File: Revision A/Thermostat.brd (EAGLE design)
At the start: 75.9 x 52.1 mm, 22 parts

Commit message: Custom Components
Designed custom components for the temperature sensor and switching
regulator.  Corrected pin 42 to 46.  Corrected some mistakes in the
schematic and re-arranged it.  Rewired the board paths to match the
original published directions.  Have not tested printing or alignment
yet.
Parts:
- removed TEMP: (no value), SparkFun-Sensors:TO-92
- removed V7815W: 7815T, linear:TO220H
- added U$1: TMP36, android-thermostat:TMP36
- added U$2: V715W-500R, android-thermostat:SWITCHINGREGULATOR
- moved 10U 7.73 mm to (61.0, 36.8), turned to 270 degrees
- moved RECT 4.02 mm to (39.4, 43.2)
- moved 100U 1.27 mm to (47.0, 36.8)
- renumbered P-42 to P-46
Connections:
- removed net N$13 (its old number): 100U.1, RECT.+, V7815W.3
- new net N$5: P-46.1, U$1.DATA-2
- net GND: now also U$1.GND-3, U$2.GND; no longer TEMP.3, V7815W.2
- net N$10: now also 10U.1, P-VIN.1, U$2.VO; no longer P-46.1, TEMP.2
- net N$11: now also U$1.VCC-1; no longer TEMP.1
- net N$12: now also 100U.1, RECT.+, U$2.VI; no longer 10U.1, P-VIN.1, V7815W.1
- net N$3: now also RECT.AC1; no longer RECT.AC2
- net P2: now also RECT.AC2; no longer RECT.AC1
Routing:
- net GND: track 132.6 -> 188.0 mm
- net N$12: track 46.0 -> 17.8 mm
- net N$5: track 0.00 -> 25.4 mm
- net N$13 (its old number): track 17.8 -> 0.00 mm
- net N$10: track 34.9 -> 17.8 mm
- net N$3: track 30.7 -> 40.6 mm
- net P2: track 69.6 -> 78.7 mm
- net N$1: track 32.1 -> 38.1 mm
- net N$4: track 8.13 -> 11.4 mm
- net N$13: track 35.1 -> 38.1 mm
- net N$15: track 30.8 -> 33.0 mm
- net N$14: track 25.7 -> 27.9 mm
- net N$7: track 15.0 -> 16.5 mm
- net N$11: track 8.89 -> 7.62 mm
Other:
- board text added: "Android Thermostat"

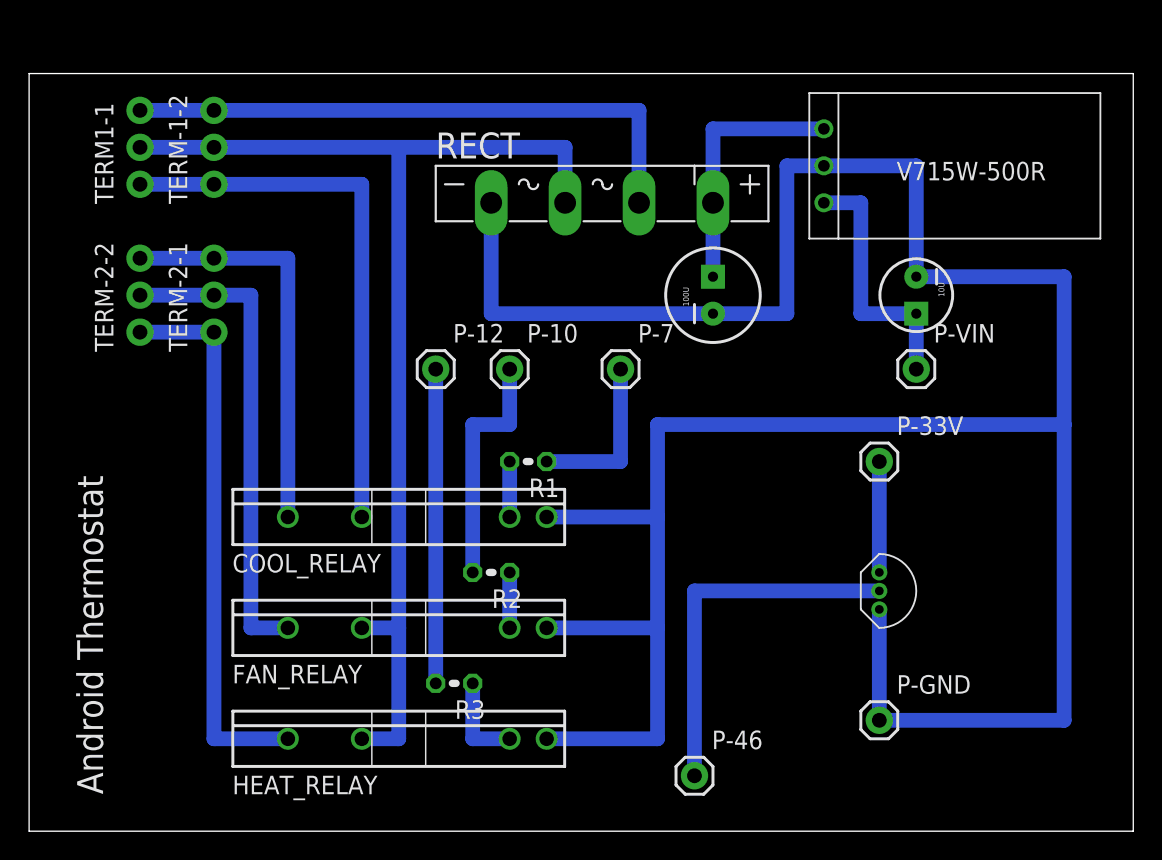
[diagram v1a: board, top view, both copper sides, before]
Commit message: Fixed Alignment
Moved all of the components to match the published board.  Revision A
should be complete now.
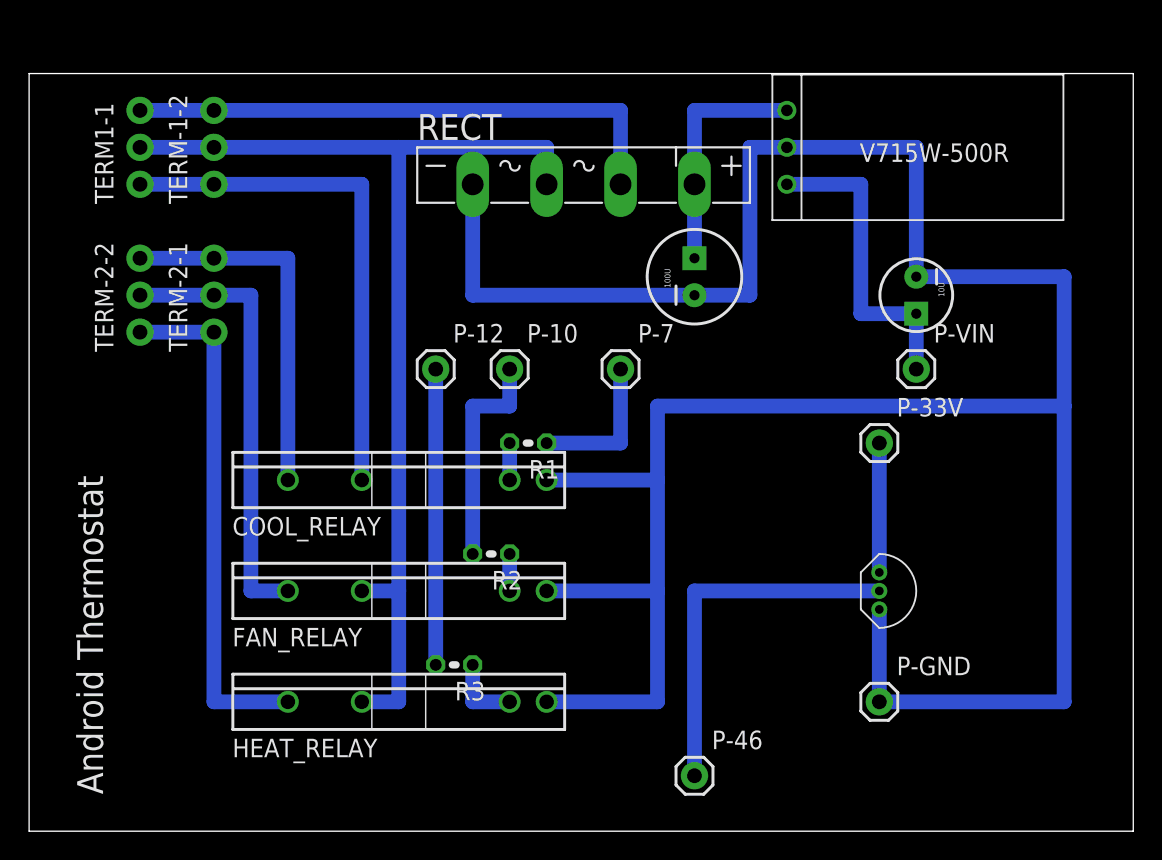
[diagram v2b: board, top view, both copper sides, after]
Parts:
- moved U$2 2.84 mm to (52.1, 47.0)
- moved FAN_RELAY 2.54 mm to (25.4, 16.5)
- moved HEAT_RELAY 2.54 mm to (25.4, 8.89)
- moved COOL_RELAY 2.54 mm to (25.4, 24.1)
- moved 100U 1.80 mm to (45.7, 38.1)
- moved RECT 1.80 mm to (38.1, 44.5)
- moved P-33V 1.27 mm to (58.4, 26.7)
- moved R1 1.27 mm to (34.3, 26.7)
- moved P-GND 1.27 mm to (58.4, 8.89)
- moved R2 1.27 mm to (31.8, 19.1)
- moved R3 1.27 mm to (29.2, 11.4)
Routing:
- net P2: track 78.7 -> 73.7 mm
- net N$10: track 17.8 -> 21.6 mm
- net N$3: track 40.6 -> 38.1 mm
- net N$15: track 33.0 -> 30.5 mm
- net N$14: track 27.9 -> 25.4 mm
- net N$1: track 38.1 -> 35.6 mm
- net N$13: track 38.1 -> 35.6 mm
- net N$4: track 11.4 -> 10.2 mm
- net N$11: track 7.62 -> 8.89 mm
- net N$6: track 3.81 -> 2.54 mm
- net N$2: track 6.35 -> 5.08 mm
- net N$8: track 21.6 -> 20.3 mm
- net N$7: track 16.5 -> 15.2 mm
- net N$9: track 3.81 -> 2.54 mm
- net N$12: track 17.8 -> 16.5 mm
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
